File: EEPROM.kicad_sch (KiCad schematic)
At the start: 22 parts, among them IC1 PCA6408A_TSSOP, IC2 AT24CS01_SOT23, U2 TPS613221A_SOT-23-5

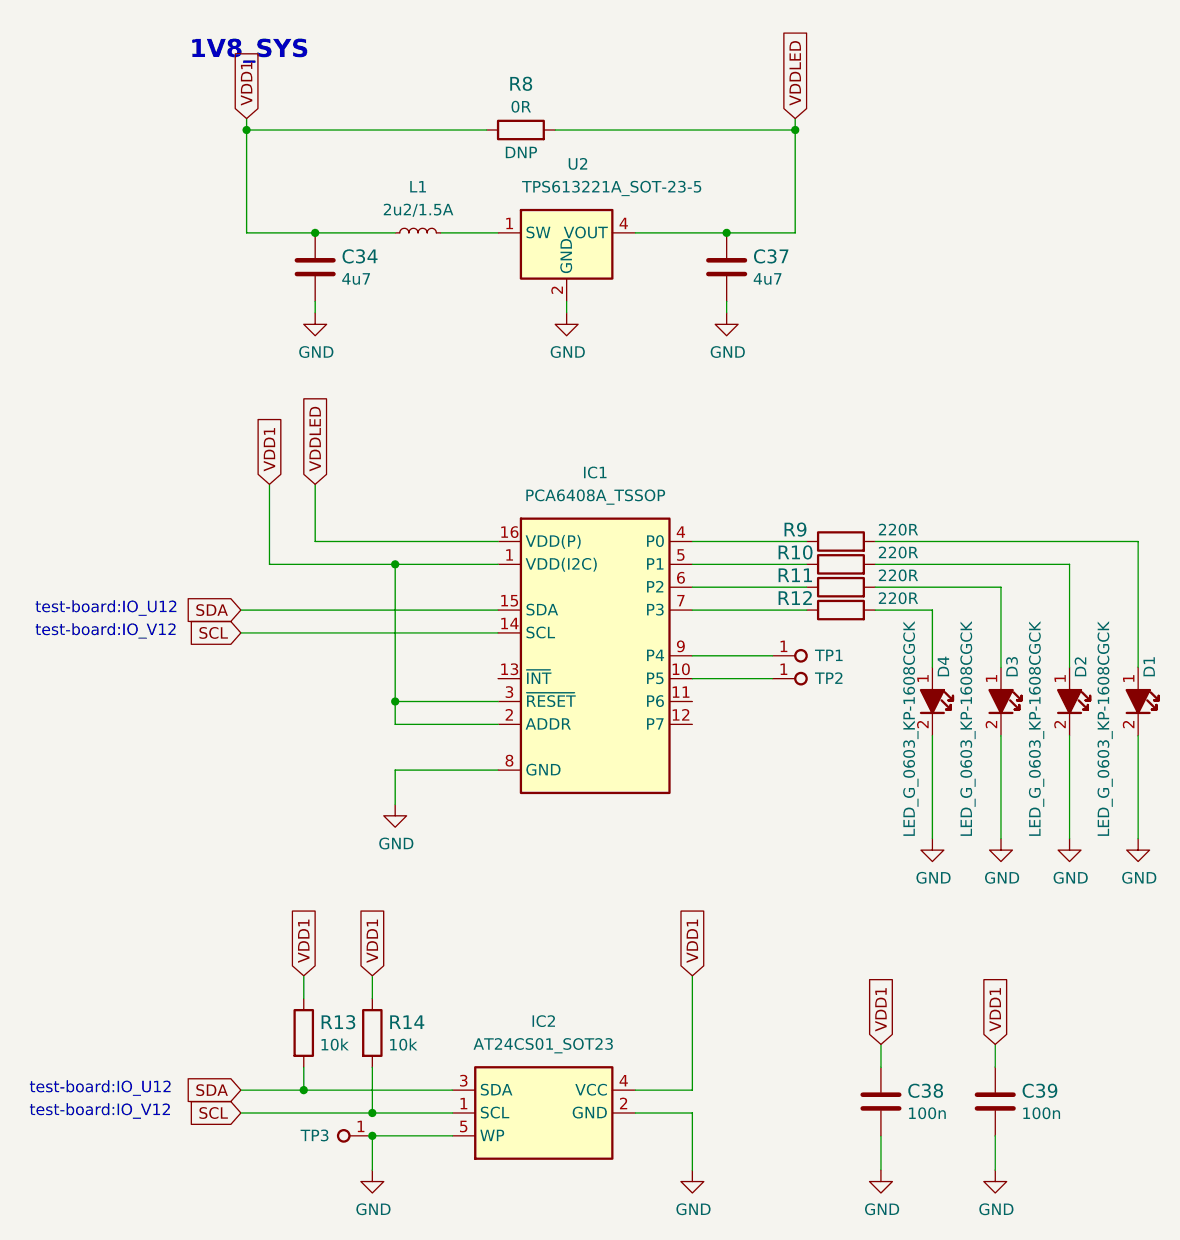
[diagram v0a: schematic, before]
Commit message: Update symbols from library, redo designators
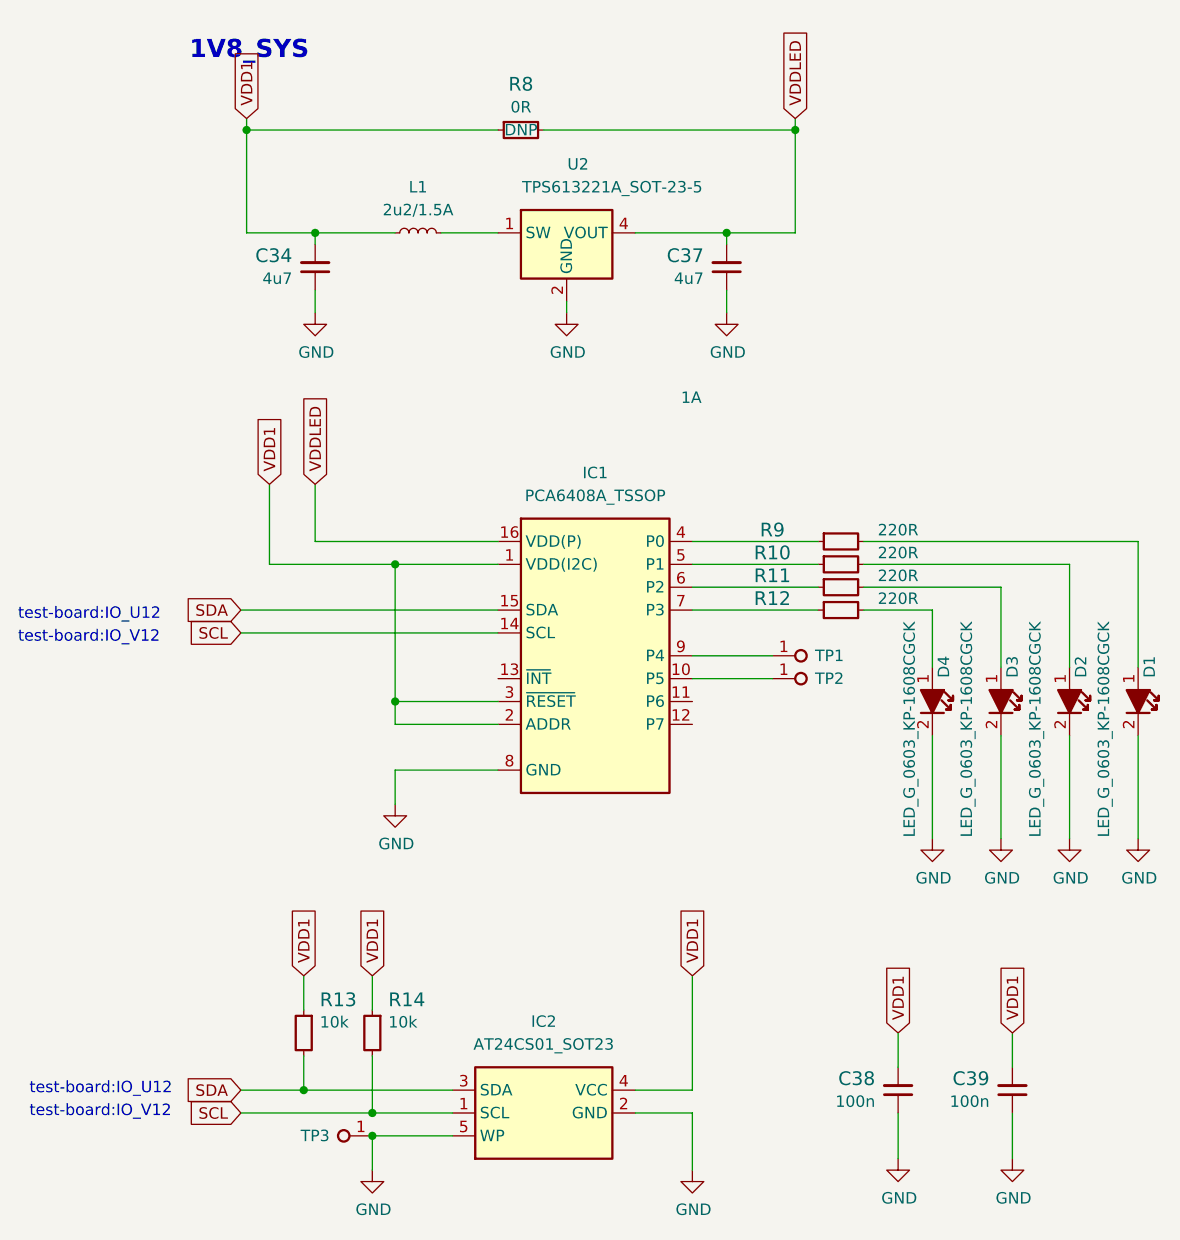
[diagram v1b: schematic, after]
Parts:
- C34, C37: Author (none) -> Antmicro; License (none) -> Apache-2.0; Manufacturer MURATA -> Murata
- C38, C39: Author (none) -> Antmicro; Dielectric (none) -> X5R; License (none) -> Apache-2.0; MPN 0402X104K6R3CT -> GRM155R61H104KE14D; Manufacturer Walsin -> Murata; Voltage (none) -> 50V
- R10, R11, R12, R9: Author (none) -> Antmicro; License (none) -> Apache-2.0; MPN ERJ2GEJ221X -> CR0402-FX-2200GLF; Manufacturer Panasonic -> Bourns; Tolerance (none) -> 1%
- R13, R14: Author (none) -> Antmicro; License (none) -> Apache-2.0; MPN CRCW040210K0FKEDHP -> CR0402-FX-1002GLF; Manufacturer VISHAY -> Bourns; Tolerance (none) -> 1%
- R8: Author (none) -> Antmicro; Current (none) -> 1A; License (none) -> Apache-2.0; Manufacturer PANASONIC -> Panasonic
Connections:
- net GND: now also C34.1, C37.1, C38.1, C39.1; no longer C34.2, C37.2, C38.2, C39.2
- net VDD1: now also C34.2, C38.2, C39.2; no longer C34.1, C38.1, C39.1
- net VDDLED: now also C37.2; no longer C37.1
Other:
- moved on the sheet: C34, C37, C38, C39
